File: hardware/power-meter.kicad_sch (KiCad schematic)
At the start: 30 parts, among them J1 USB_C_Receptacle_USB2.0_16P, J2 USB_C_Receptacle_USB2.0_16P, J3 OLED, J4 PROG, J5 IN+, J6 IN-, J7 OUT+, J8 OUT-, SW1 SW_Push, SW2 SW_Push, U1 AP2112K-3.3, U2 STM32F103CBTx, U3 INA213BIDCKT, U4 ADS1220xPW

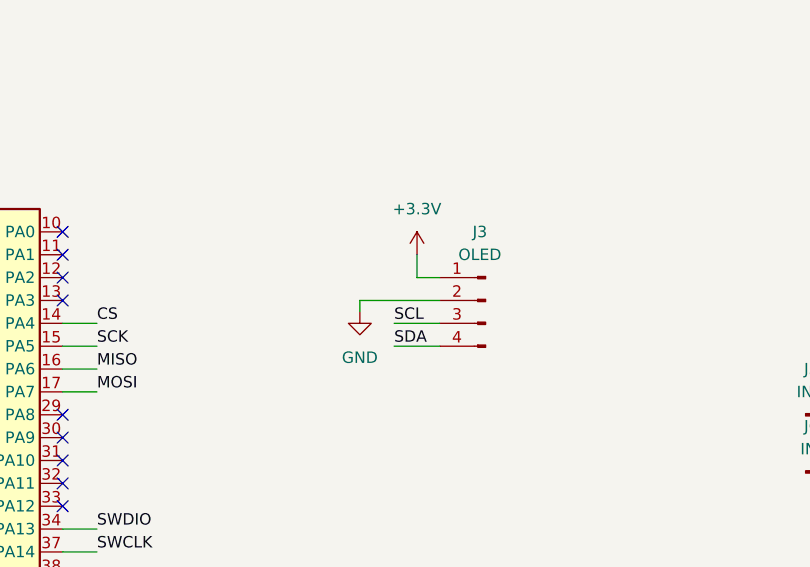
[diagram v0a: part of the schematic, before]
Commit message: OLED power fixed
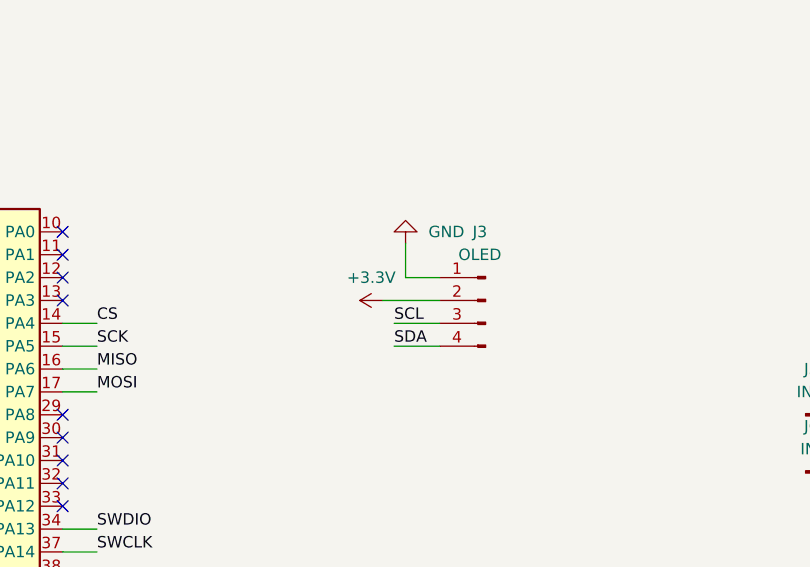
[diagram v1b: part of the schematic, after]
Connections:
- net +3.3V: now also J3.2 (Pin_2); no longer J3.1 (Pin_1)
- net GND: now also J3.1 (Pin_1); no longer J3.2 (Pin_2)
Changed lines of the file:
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@@
 	(wire
 		(pts
+			(xy 156.21 95.25) (xy 162.56 95.25)
+		)
+		(stroke
+			(width 0)
+			(type default)
+		)
+	)
+	(wire
+		(pts
 			(xy 100.33 82.55) (xy 100.33 80.01)
 		)
@@
 	(wire
 		(pts
-			(xy 160.02 92.71) (xy 160.02 90.17)
-		)
-		(stroke
-			(width 0)
-			(type default)
-		)
-	)
-	(wire
-		(pts
 			(xy 207.01 63.5) (xy 207.01 66.04)
 		)
@@
 	(wire
 		(pts
-			(xy 162.56 92.71) (xy 160.02 92.71)
-		)
-		(stroke
-			(width 0)
-			(type default)
-		)
-	)
-	(wire
-		(pts
 			(xy 78.74 27.94) (xy 81.28 27.94)
 		)
@@
 	(wire
 		(pts
-			(xy 162.56 95.25) (xy 153.67 95.25)
-		)
-		(stroke
-			(width 0)
-			(type default)
-		)
-	)
-	(wire
-		(pts
 			(xy 33.02 64.77) (xy 33.02 67.31)
 		)
@@
 	(wire
 		(pts
-			(xy 153.67 95.25) (xy 153.67 96.52)
-		)
-		(stroke
-			(width 0)
-			(type default)
-		)
-	)
-	(wire
-		(pts
 			(xy 53.34 124.46) (xy 53.34 125.73)
 		)
@@
 	(wire
 		(pts
+			(xy 158.75 88.9) (xy 158.75 92.71)
+		)
+		(stroke
+			(width 0)
+			(type default)
+		)
+	)
+	(wire
+		(pts
 			(xy 105.41 78.74) (xy 105.41 80.01)
 		)
@@
 	(wire
 		(pts
+			(xy 158.75 92.71) (xy 162.56 92.71)
+		)
+		(stroke
+			(width 0)
+			(type default)
+		)
+	)
+	(wire
+		(pts
 			(xy 30.48 124.46) (xy 30.48 125.73)
 		)
@@
 	(symbol
 		(lib_id "power:GND")
-		(at 153.67 96.52 0)
+		(at 158.75 88.9 180)
 		(unit 1)
 		(exclude_from_sim no)
@@
 		(fields_autoplaced yes)
 		(property "Reference" "#PWR031"
-			(at 153.67 102.87 0)
+			(at 158.75 82.55 0)
 			(effects
 				(font
@@
 		)
 		(property "Value" "GND"
-			(at 153.67 101.6 0)
+			(at 161.29 87.6299 0)
 			(effects
 				(font
 					(size 1.27 1.27)
 				)
+				(justify right)
 			)
 		)
 		(property "Footprint" ""
-			(at 153.67 96.52 0)
+			(at 158.75 88.9 0)
 			(effects
 				(font
@@
 		)
 		(property "Datasheet" ""
-			(at 153.67 96.52 0)
+			(at 158.75 88.9 0)
 			(effects
 				(font
@@
 		)
 		(property "Description" "Power symbol creates a global label with name \"GND\" , ground"
-			(at 153.67 96.52 0)
+			(at 158.75 88.9 0)
 			(effects
 				(font
@@
 	(symbol
 		(lib_id "power:+3.3V")
-		(at 160.02 90.17 0)
+		(at 156.21 95.25 90)
 		(unit 1)
 		(exclude_from_sim no)
@@
 		(fields_autoplaced yes)
 		(property "Reference" "#PWR030"
-			(at 160.02 93.98 0)
+			(at 160.02 95.25 0)
 			(effects
 				(font
@@
 		)
 		(property "Value" "+3.3V"
-			(at 160.02 85.09 0)
+			(at 154.94 92.71 90)
 			(effects
 				(font
@@
 		)
 		(property "Footprint" ""
-			(at 160.02 90.17 0)
+			(at 156.21 95.25 0)
 			(effects
 				(font
@@
 		)
 		(property "Datasheet" ""
-			(at 160.02 90.17 0)
+			(at 156.21 95.25 0)
 			(effects
 				(font
@@
 		)
 		(property "Description" "Power symbol creates a global label with name \"+3.3V\""
-			(at 160.02 90.17 0)
+			(at 156.21 95.25 0)
 			(effects
 				(font

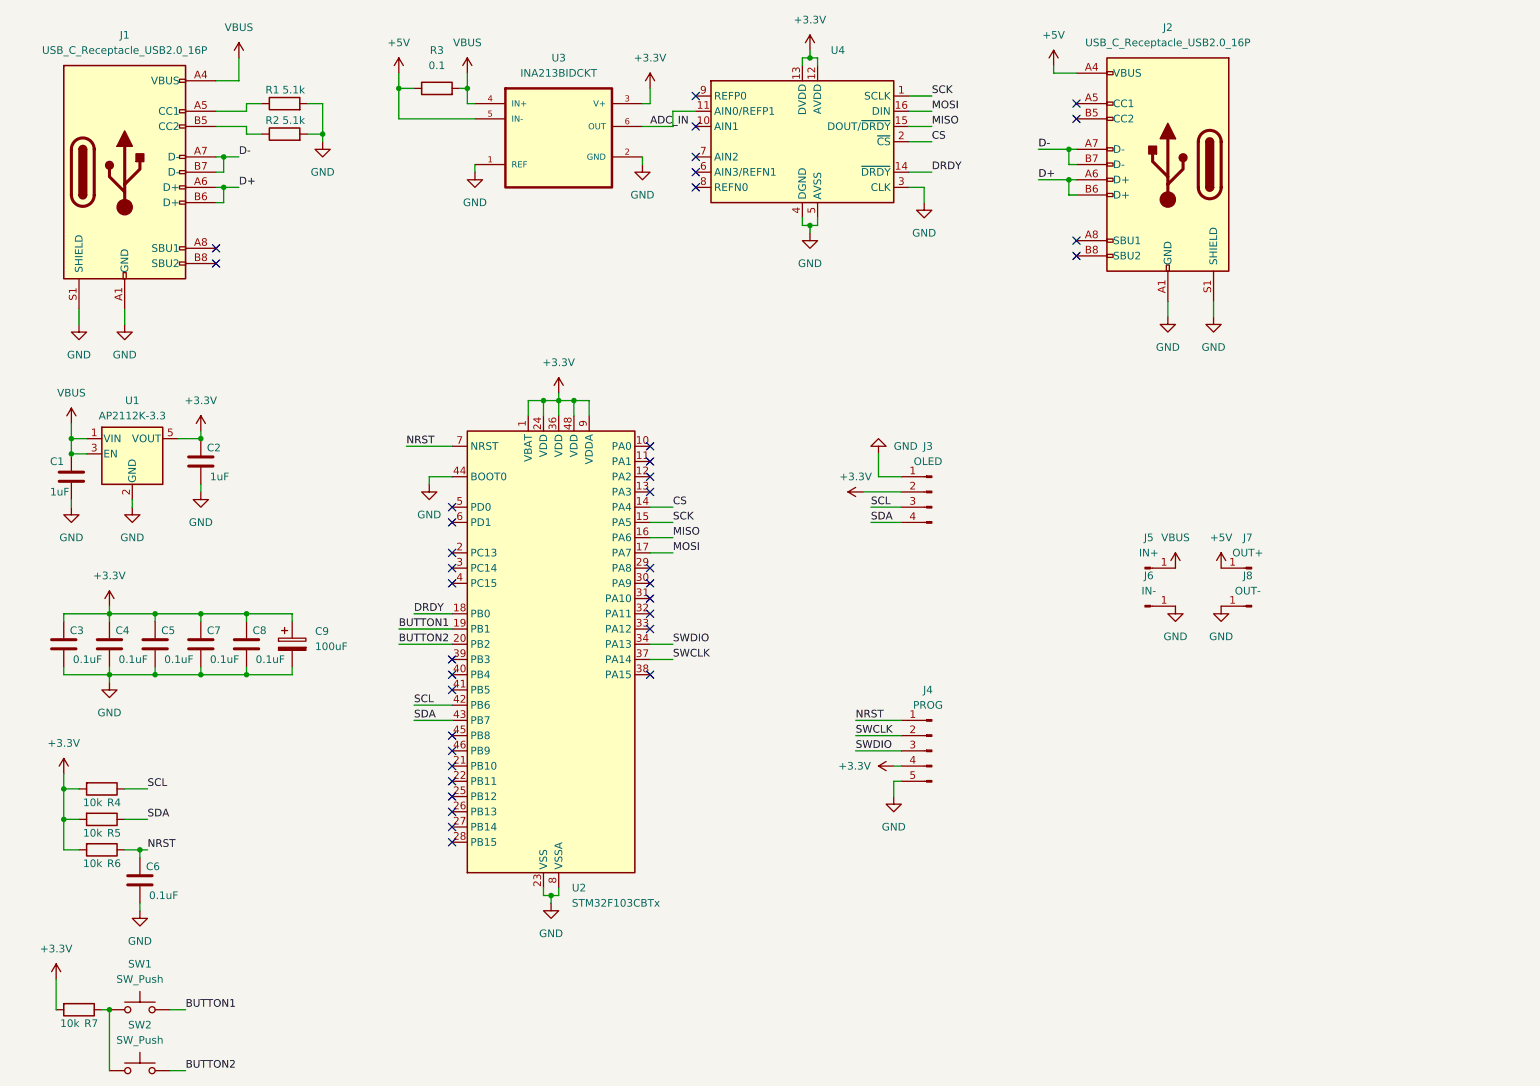
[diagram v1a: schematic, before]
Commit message: feat: v2
Consolidate all work related to hardware revision v2 and firmware migration for that revision.

Hardware scope:

- Redesign PCB/schematic from v1 to v2 with updated component and connectivity decisions.

- Add STM32G431 symbol/library assets used by the new design.

- Integrate board-level corrections performed after first v2 routing pass.

Firmware scope:

- Migrate firmware target to STM32G431 platform and board configuration.

- Update build configuration and platform definitions for the new MCU/board.

- Adapt application logic to v2 hardware behavior and interfaces.

- Refactor firmware from monolithic source into focused modules (adc/config/display/util).

- Apply stabilization fixes after modular split.

Why:

- Represent v2 as a coherent generation change (hardware redesign + firmware migration).

- Keep migration rationale and resulting architecture in one clear historical checkpoint.
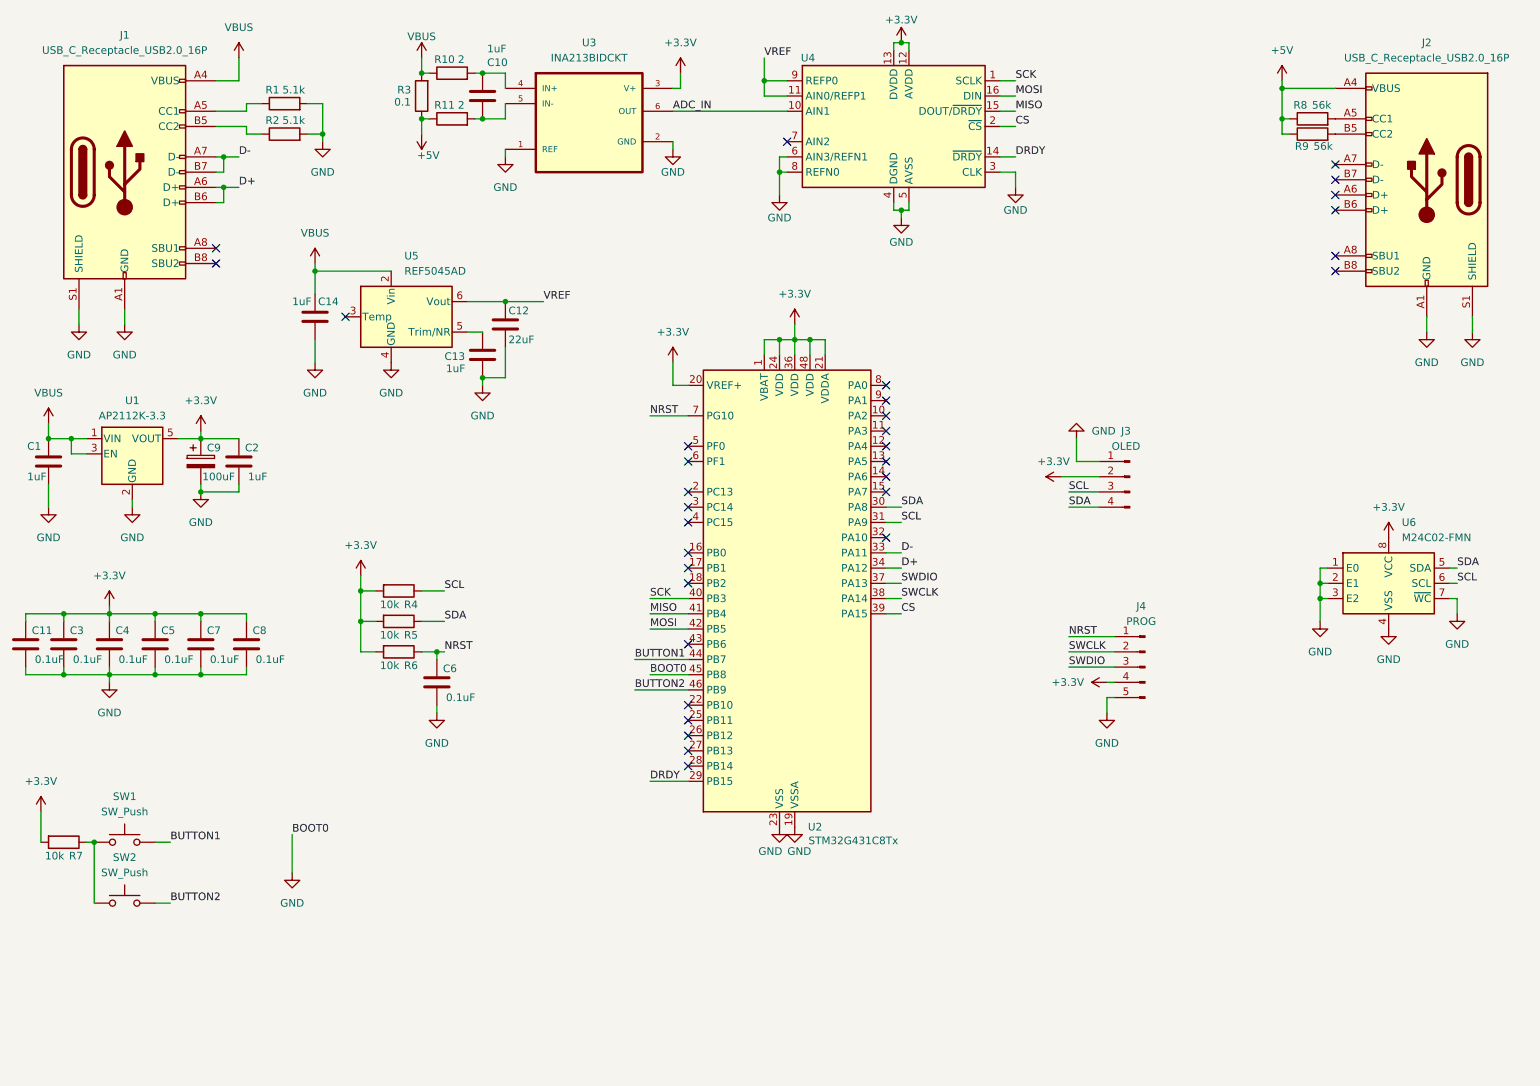
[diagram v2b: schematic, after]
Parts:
- removed J5: IN+, Connector_PinSocket_2.54mm:PinSocket_1x01_P2.54mm_Vertical, symbol Connector:Conn_01x01_Pin
- removed J6: IN-, Connector_PinSocket_2.54mm:PinSocket_1x01_P2.54mm_Vertical, symbol Connector:Conn_01x01_Pin
- removed J7: OUT+, Connector_PinSocket_2.54mm:PinSocket_1x01_P2.54mm_Vertical, symbol Connector:Conn_01x01_Pin
- removed J8: OUT-, Connector_PinSocket_2.54mm:PinSocket_1x01_P2.54mm_Vertical, symbol Connector:Conn_01x01_Pin
- removed U2: STM32F103CBTx, Package_QFP:LQFP-48_7x7mm_P0.5mm, symbol MCU_ST_STM32F1:STM32F103CBTx
- added C10, C13, C14: 1uF, Capacitor_SMD:C_0603_1608Metric, symbol Device:C
- added C11: 0.1uF, Capacitor_SMD:C_0603_1608Metric, symbol Device:C
- added C12: 22uF, Capacitor_SMD:C_0603_1608Metric, symbol Device:C
- added R10, R11: 2, Resistor_SMD:R_0603_1608Metric, symbol Device:R
- added R8, R9: 56k, Resistor_SMD:R_0603_1608Metric, symbol Device:R
- added U2: STM32G431C8Tx, Package_QFP:LQFP-48_7x7mm_P0.5mm, symbol MCU_ST_STM32G4:STM32G431C8Tx
- added U5: REF5045AD, Package_SO:SOIC-8_3.9x4.9mm_P1.27mm, symbol Reference_Voltage:REF5040AD
- added U6: M24C02-FMN, Package_SO:SOIC-8_3.9x4.9mm_P1.27mm, symbol Memory_EEPROM:M24C02-FMN
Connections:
- net +3.3V: now also C11.1, U2.1 (VBAT), U2.20 (VREF+), U2.21 (VDDA), U2.24 (VDD), U2.36 (VDD), U2.48 (VDD), U6.8 (VCC)
- net +5V: now also R11.1, R8.1, R9.1; no longer U3.5 (IN-)
- net ADC_IN: now also U4.10 (AIN1); no longer U4.11 (AIN0/REFP1)
- net BUTTON1: now also U2.44 (PB7)
- net BUTTON2: now also U2.46 (PB9)
- net CS: now also U2.39 (PA15)
- net D+: now also U2.34 (PA12); no longer J2.A6 (D+), J2.B6 (D+)
- net D-: now also U2.33 (PA11); no longer J2.A7 (D-), J2.B7 (D-)
- net DRDY: now also U2.29 (PB15)
- net GND: now also U4.6 (AIN3/REFN1), U4.8 (REFN0), C11.2, C12.2, C13.2, C14.2, U2.19 (VSSA), U2.23 (VSS), U2.35 (VSS), U2.45 (PB8), U2.47 (VSS), U5.4 (GND), U6.1 (E0), U6.2 (E1), U6.3 (E2), U6.4 (VSS), U6.7 (~{WC})
- net MISO: now also U2.41 (PB4)
- net MOSI: now also U2.42 (PB5)
- net NRST: now also U2.7 (PG10)
- net SCK: now also U2.40 (PB3)
- net SCL: now also U2.31 (PA9), U6.6 (SCL)
- net SDA: now also U2.30 (PA8), U6.5 (SDA)
- net SWCLK: now also U2.38 (PA14)
- net SWDIO: now also U2.37 (PA13)
- net VBUS: now also C14.1, R10.1, U5.2 (Vin); no longer U3.4 (IN+)
- net VREF: now reaches U4.9 (REFP0)
- net VREF: now also U4.11 (AIN0/REFP1), C12.1, U5.6 (Vout)
- net at J2.A5 (CC1): now also R8.2
- net at J2.B5 (CC2): now also R9.2
- new net: C10.1, R10.2, U3.4 (IN+)
- new net: C10.2, R11.2, U3.5 (IN-)
- new net: C13.1, U5.5 (Trim/NR)
- no-connect marks 37 -> 33
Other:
- title: (none) -> Power Meter
- moved on the sheet: C1, C2, C6, C9, J2, J3, J4, R3, R4, R5, R6, R7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
